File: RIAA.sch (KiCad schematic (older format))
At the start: 34 parts, among them U1 NE5532

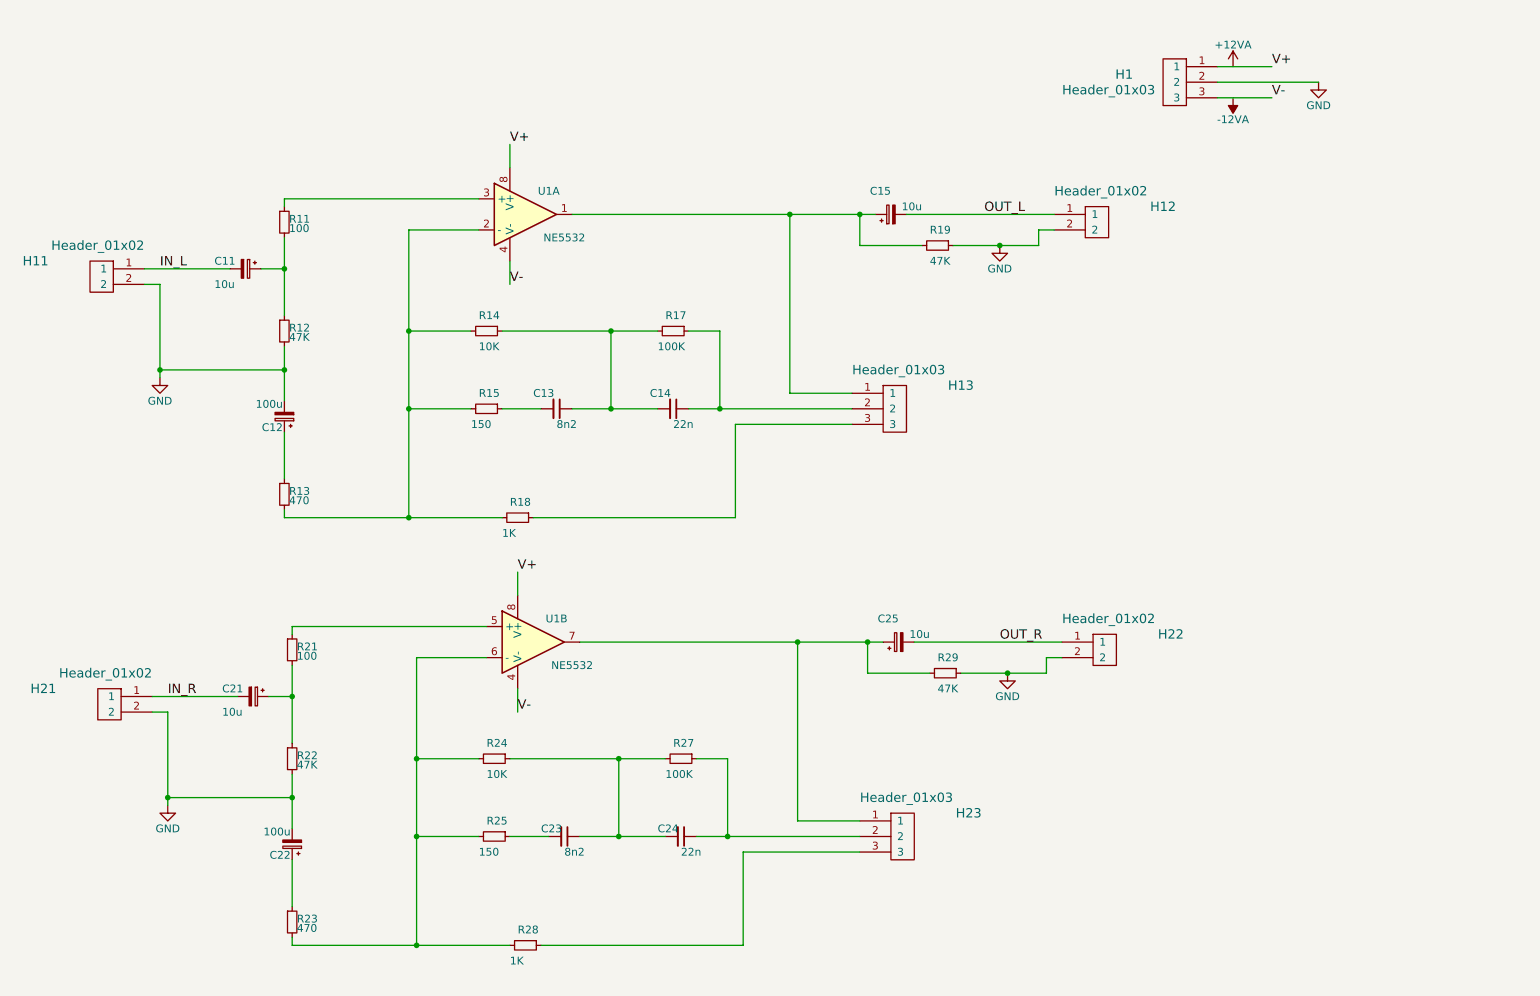
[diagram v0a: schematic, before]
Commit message: Partial update to add Molex connector for the switch connection
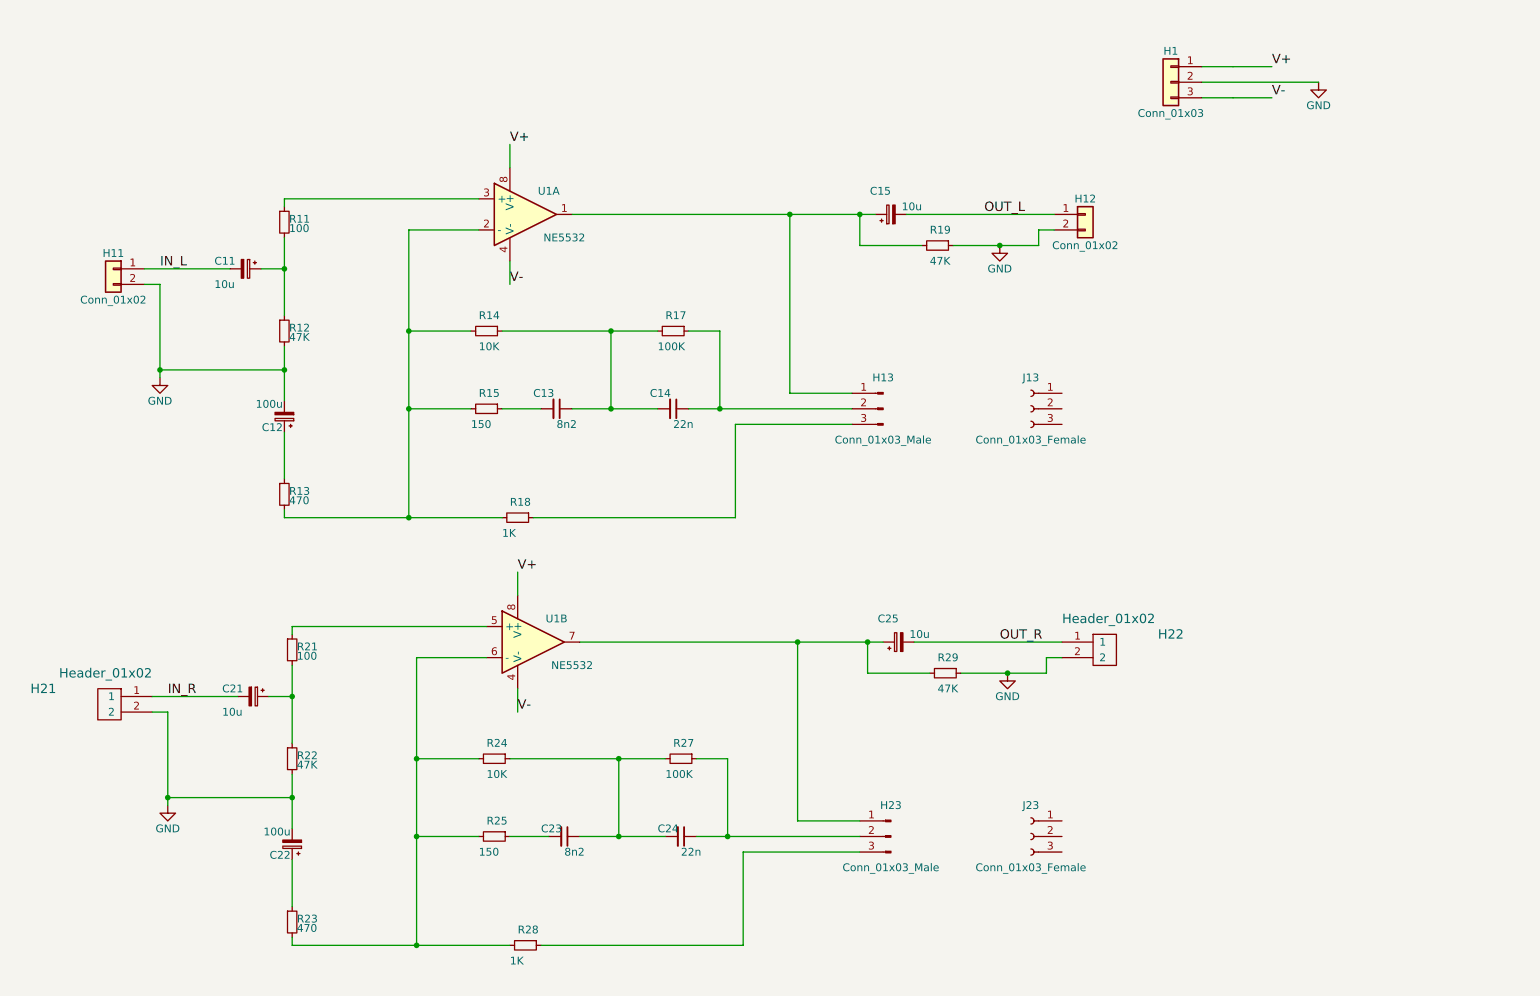
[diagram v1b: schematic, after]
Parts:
- removed H1, H13, H23: Header_01x03, Pin_Headers:Pin_Header_Straight_1x03, symbol Header_01x03
- removed H11, H12: Header_01x02, Pin_Headers:Pin_Header_Straight_1x02, symbol Header_01x02
- added H1: Conn_01x03, symbol Conn_01x03
- added H11, H12: Conn_01x02, symbol Conn_01x02
- added H13, H23: Conn_01x03_Male, Connectors_Molex:Molex_KK-6410-03_03x2.54mm_Straight, symbol Conn_01x03_Male
- added J13, J23: Conn_01x03_Female, symbol Conn_01x03_Female
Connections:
- net GND: now also H1.2 (Pin_2), H11.2 (Pin_2), H12.2 (Pin_2)
- net IN_L: now also H11.1 (Pin_1)
- net OUT_L: now also H12.1 (Pin_1)
- net V+: now also H1.1 (Pin_1)
- net V-: now also H1.3 (Pin_3)
- net at C15.1, R19.2, U1.1: now also H13.1 (Pin_1)
- net at C14.1, R17.1: now also H13.2 (Pin_2)
- net at R18.1: now also H13.3 (Pin_3)
- net at C25.1, R29.2, U1.7: now also H23.1 (Pin_1)
- net at C24.1, R27.1: now also H23.2 (Pin_2)
- net at R28.1: now also H23.3 (Pin_3)

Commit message: Add OpAmp references
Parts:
- U1: Description (none) -> Operational Amplifiers - Op Amps Dual Low Noise; Distributor (none) -> Mouser; Distributor Part # (none) -> 595-NE5532P; Manufacturer (none) -> Texas Instruments; Package (none) -> 8-PDIP
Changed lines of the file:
@@
 F 1 "NE5532" H 4550 1950 50  0000 C CNN
 F 2 "Housings_DIP:DIP-8_W7.62mm_LongPads" H 4300 2100 50  0001 C CNN
-F 3 "" H 4300 2100 50  0000 C CNN
+F 3 "http://www.ti.com/lit/gpn/ne5532" H 4300 2100 50  0001 C CNN
 F 4 "NE5532P" H 4300 2100 60  0001 C CNN "Mfg_Part_No"
+F 5 "Operational Amplifiers - Op Amps Dual Low Noise" H 4300 2100 60  0001 C CNN "Description"
+F 6 "Texas Instruments" H 4300 2100 60  0001 C CNN "Manufacturer"
+F 7 "Mouser" H 4300 2100 60  0001 C CNN "Distributor"
+F 8 "595-NE5532P" H 4300 2100 60  0001 C CNN "Distributor Part #"
+F 9 "8-PDIP" H 4300 2100 60  0001 C CNN "Package"
 	1    4300 2100
 	1    0    0    -1
@@
 F 4 "CCF07470RGKE36CCF07470RGKE36CCF07470RGKE36" H 2800 6650 60  0001 C CNN "Mfg_Part_No"
 	1    2800 6650
-	1    0    0    -1
-$EndComp
-$Comp
-L NE5532 U1
-U 2 1 571FB127
-P 4350 4850
-F 0 "U1" H 4500 5000 50  0000 C CNN
-F 1 "NE5532" H 4600 4700 50  0000 C CNN
-F 2 "Housings_DIP:DIP-8_W7.62mm_LongPads" H 4350 4850 50  0001 C CNN
-F 3 "" H 4350 4850 50  0000 C CNN
-F 4 "NE5532P" H 4350 4850 60  0001 C CNN "Mfg_Part_No"
-	2    4350 4850
 	1    0    0    -1
 $EndComp
@@
 	-1   0    0    -1
 $EndComp
+$Comp
+L NE5532 U1
+U 2 1 5A14798A
+P 4350 4850
+F 0 "U1" H 4500 5000 50  0000 C CNN
+F 1 "NE5532" H 4600 4700 50  0000 C CNN
+F 2 "Housings_DIP:DIP-8_W7.62mm_LongPads" H 4350 4850 50  0001 C CNN
+F 3 "http://www.ti.com/lit/gpn/ne5532" H 4350 4850 50  0001 C CNN
+F 4 "NE5532P" H 4350 4850 60  0001 C CNN "Mfg_Part_No"
+F 5 "Operational Amplifiers - Op Amps Dual Low Noise" H 4350 4850 60  0001 C CNN "Description"
+F 6 "Texas Instruments" H 4350 4850 60  0001 C CNN "Manufacturer"
+F 7 "Mouser" H 4350 4850 60  0001 C CNN "Distributor"
+F 8 "595-NE5532P" H 4350 4850 60  0001 C CNN "Distributor Part #"
+F 9 "8-PDIP" H 4350 4850 60  0001 C CNN "Package"
+	2    4350 4850
+	1    0    0    -1
+$EndComp
 $EndSCHEMATC

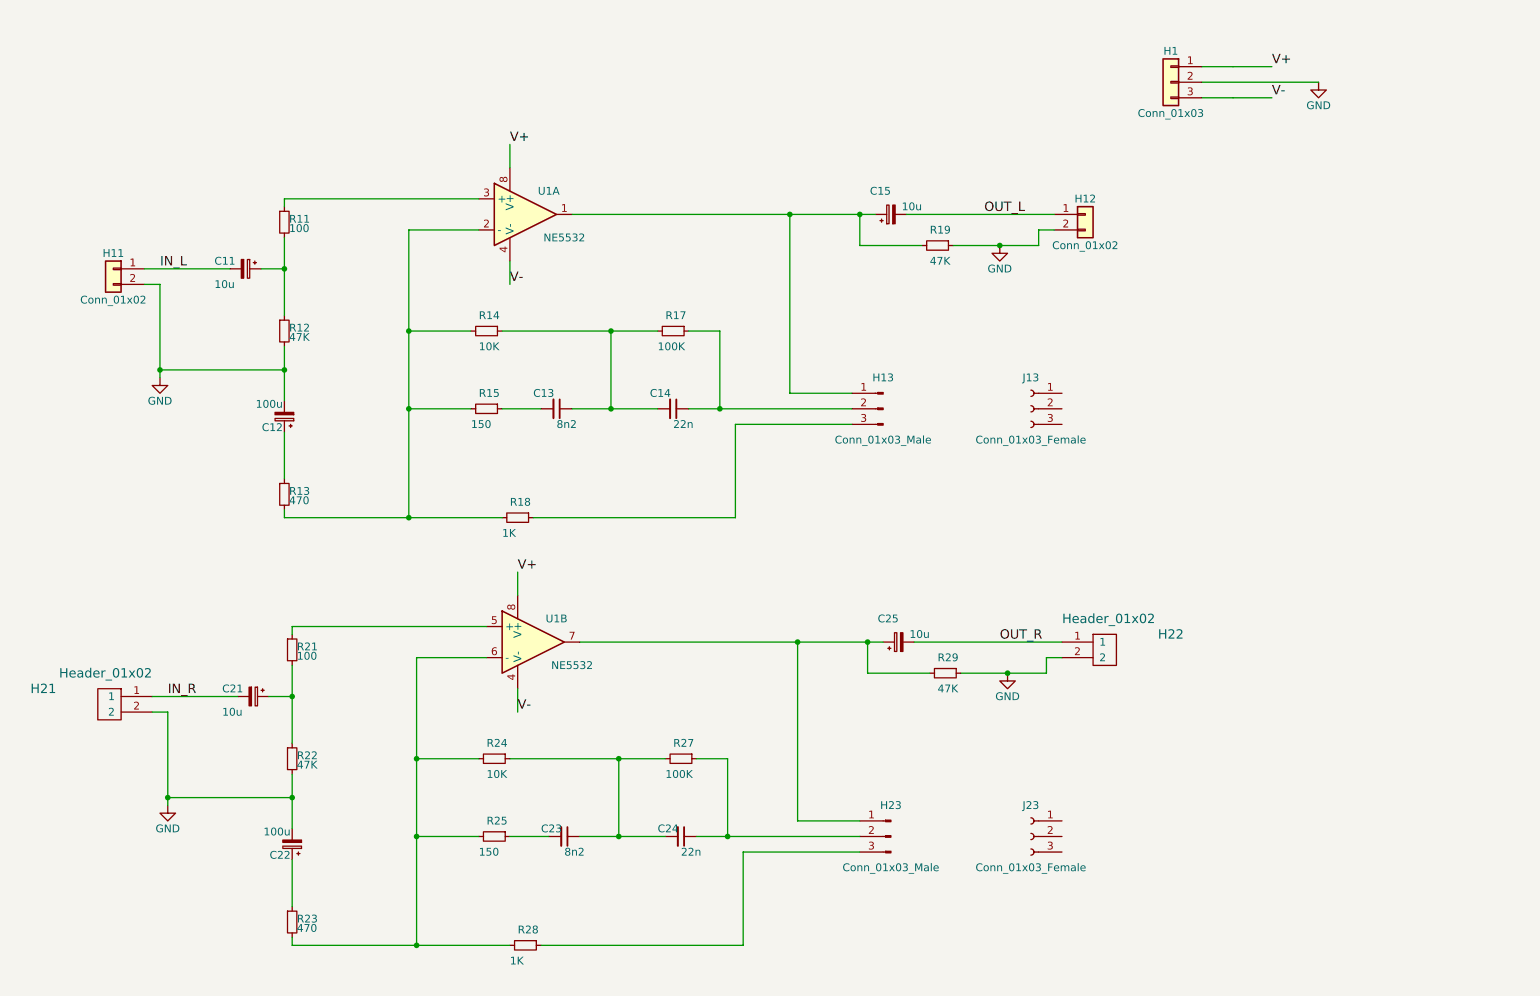
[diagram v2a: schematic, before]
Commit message: Adding switches for line/phono input commutation
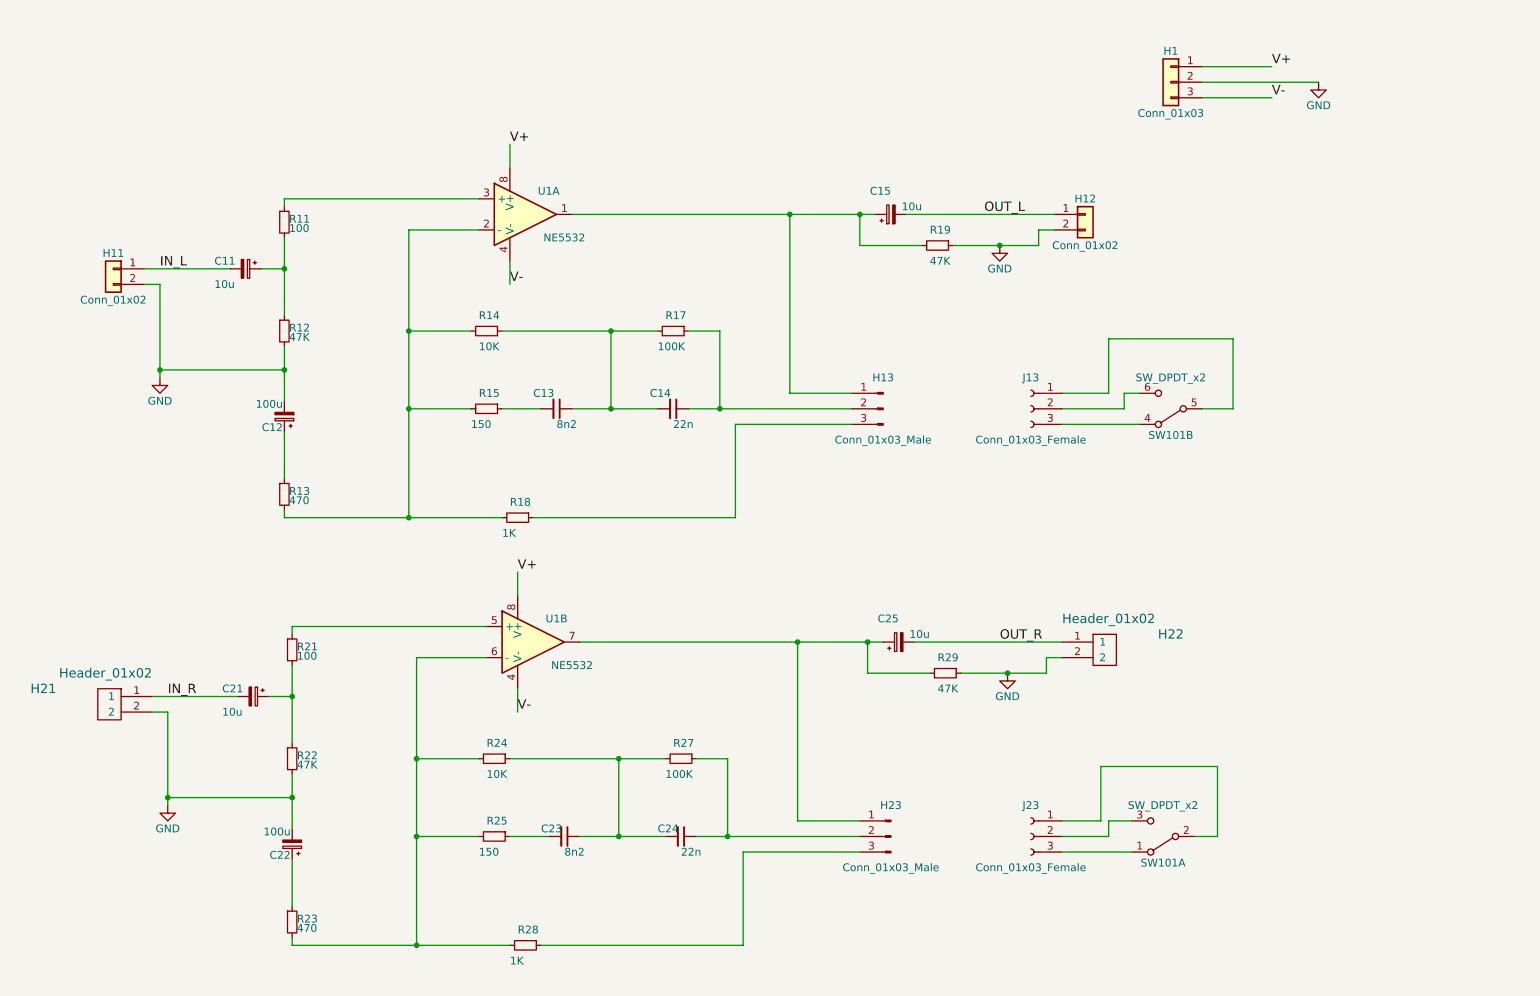
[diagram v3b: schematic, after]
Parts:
- added SW101: SW_DPDT_x2, symbol SW_DPDT_x2
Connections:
- net at J23.1 (Pin_1): now also SW101.2 (B)
- net at J23.2 (Pin_2): now also SW101.3 (C)
- net at J23.3 (Pin_3): now also SW101.1 (A)
- net at J13.1 (Pin_1): now also SW101.5 (B)
- net at J13.2 (Pin_2): now also SW101.6 (C)
- net at J13.3 (Pin_3): now also SW101.4 (A)
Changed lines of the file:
@@
 LIBS:contrib
 LIBS:valves
+LIBS:switches
 LIBS:RIAA-cache
 EELAYER 25 0
@@
 $EndComp
 $Comp
-L GND #PWR01
+L GND #PWR101
 U 1 1 571FAC30
 P 1950 3150
-F 0 "#PWR01" H 1950 2900 50  0001 C CNN
+F 0 "#PWR101" H 1950 2900 50  0001 C CNN
 F 1 "GND" H 1950 3000 50  0000 C CNN
 F 2 "" H 1950 3150 50  0000 C CNN
@@
 	1850 2550 1950 2550
 Wire Wire Line
-	1950 2550 1950 3100
-Wire Wire Line
-	1950 3100 1950 3150
+	1950 2550 1950 3150
 Wire Wire Line
 	1850 2450 2400 2450
@@
 	2600 2450 2750 2450
 Wire Wire Line
-	2750 2250 2750 2450
-Wire Wire Line
-	2750 2450 2750 2750
+	2750 2250 2750 2750
 Connection ~ 2750 2450
 Wire Wire Line
-	2750 2950 2750 3100
-Wire Wire Line
-	2750 3100 2750 3300
+	2750 2950 2750 3300
 Wire Wire Line
 	2750 3500 2750 3800
@@
 $EndComp
 Wire Wire Line
-	5350 3350 5550 3350
-Wire Wire Line
-	5550 3350 6400 3350
+	5350 3350 6400 3350
 Wire Wire Line
 	5350 2850 5550 2850
@@
 Connection ~ 5550 3350
 Wire Wire Line
-	4150 2850 4850 2850
-Wire Wire Line
-	4850 2850 5150 2850
-Wire Wire Line
-	4600 3350 4850 3350
-Wire Wire Line
-	4850 3350 5150 3350
+	4150 2850 5150 2850
+Wire Wire Line
+	4600 3350 5150 3350
 Wire Wire Line
 	4850 3350 4850 2850
@@
 	3950 2850 3550 2850
 Wire Wire Line
-	3550 2200 3550 2850
-Wire Wire Line
-	3550 2850 3550 3350
-Wire Wire Line
-	3550 3350 3550 4050
+	3550 2200 3550 4050
 Wire Wire Line
 	3550 3350 3950 3350
@@
 	2750 4000 2750 4050
 Wire Wire Line
-	2750 4050 3550 4050
-Wire Wire Line
-	3550 4050 4150 4050
+	2750 4050 4150 4050
 Wire Wire Line
 	4350 4050 5650 4050
@@
 	5650 3450 6400 3450
 Wire Wire Line
-	8650 1150 8850 1150
-Wire Wire Line
-	8850 1150 9100 1150
-Wire Wire Line
-	8650 1350 8850 1350
-Wire Wire Line
-	8850 1350 9100 1350
+	8650 1150 9100 1150
+Wire Wire Line
+	8650 1350 9100 1350
 Text Label 9100 1150 0    60   ~ 0
 V+
@@
 	2750 2000 4000 2000
 Wire Wire Line
-	4600 2100 6000 2100
-Wire Wire Line
-	6000 2100 6450 2100
-Wire Wire Line
-	6450 2100 6550 2100
+	4600 2100 6550 2100
 Wire Wire Line
 	6000 2100 6000 3250
@@
 $EndComp
 $Comp
-L GND #PWR04
+L GND #PWR103
 U 1 1 571FAC4B
 P 7350 2300
-F 0 "#PWR04" H 7350 2050 50  0001 C CNN
+F 0 "#PWR103" H 7350 2050 50  0001 C CNN
 F 1 "GND" H 7350 2150 50  0000 C CNN
 F 2 "" H 7350 2300 50  0000 C CNN
@@
 $EndComp
 Wire Wire Line
-	7050 2300 7350 2300
-Wire Wire Line
-	7350 2300 7600 2300
+	7050 2300 7600 2300
 Wire Wire Line
 	7700 2200 7600 2200
@@
 $EndComp
 $Comp
-L GND #PWR05
+L GND #PWR102
 U 1 1 571FB0FD
 P 2000 5900
-F 0 "#PWR05" H 2000 5650 50  0001 C CNN
+F 0 "#PWR102" H 2000 5650 50  0001 C CNN
 F 1 "GND" H 2000 5750 50  0000 C CNN
 F 2 "" H 2000 5900 50  0000 C CNN
@@
 	1900 5300 2000 5300
 Wire Wire Line
-	2000 5300 2000 5850
-Wire Wire Line
-	2000 5850 2000 5900
+	2000 5300 2000 5900
 Wire Wire Line
 	1900 5200 2450 5200
@@
 	2650 5200 2800 5200
 Wire Wire Line
-	2800 5000 2800 5200
-Wire Wire Line
-	2800 5200 2800 5500
+	2800 5000 2800 5500
 Connection ~ 2800 5200
 Wire Wire Line
-	2800 5700 2800 5850
-Wire Wire Line
-	2800 5850 2800 6050
+	2800 5700 2800 6050
 Wire Wire Line
 	2800 6250 2800 6550
@@
 $EndComp
 Wire Wire Line
-	5400 6100 5600 6100
-Wire Wire Line
-	5600 6100 6450 6100
+	5400 6100 6450 6100
 Wire Wire Line
 	5400 5600 5600 5600
@@
 Connection ~ 5600 6100
 Wire Wire Line
-	4200 5600 4900 5600
-Wire Wire Line
-	4900 5600 5200 5600
-Wire Wire Line
-	4650 6100 4900 6100
-Wire Wire Line
-	4900 6100 5200 6100
+	4200 5600 5200 5600
+Wire Wire Line
+	4650 6100 5200 6100
 Wire Wire Line
 	4900 6100 4900 5600
@@
 	4000 5600 3600 5600
 Wire Wire Line
-	3600 4950 3600 5600
-Wire Wire Line
-	3600 5600 3600 6100
-Wire Wire Line
-	3600 6100 3600 6800
+	3600 4950 3600 6800
 Wire Wire Line
 	3600 6100 4000 6100
@@
 	2800 6750 2800 6800
 Wire Wire Line
-	2800 6800 3600 6800
-Wire Wire Line
-	3600 6800 4200 6800
+	2800 6800 4200 6800
 Wire Wire Line
 	4400 6800 5700 6800
@@
 	2800 4750 4050 4750
 Wire Wire Line
-	4650 4850 6050 4850
-Wire Wire Line
-	6050 4850 6500 4850
-Wire Wire Line
-	6500 4850 6600 4850
+	4650 4850 6600 4850
 Wire Wire Line
 	6050 4850 6050 6000
@@
 $EndComp
 $Comp
-L GND #PWR06
+L GND #PWR104
 U 1 1 571FB199
 P 7400 5050
-F 0 "#PWR06" H 7400 4800 50  0001 C CNN
+F 0 "#PWR104" H 7400 4800 50  0001 C CNN
 F 1 "GND" H 7400 4900 50  0000 C CNN
 F 2 "" H 7400 5050 50  0000 C CNN
@@
 $EndComp
 Wire Wire Line
-	7100 5050 7400 5050
-Wire Wire Line
-	7400 5050 7650 5050
+	7100 5050 7650 5050
 Wire Wire Line
 	7750 4950 7650 4950
@@
 	6800 4850 7750 4850
 $Comp
-L GND #PWR07
+L GND #PWR105
 U 1 1 5724D462
 P 9400 1250
-F 0 "#PWR07" H 9400 1000 50  0001 C CNN
+F 0 "#PWR105" H 9400 1000 50  0001 C CNN
 F 1 "GND" H 9400 1100 50  0000 C CNN
 F 2 "" H 9400 1250 50  0000 C CNN
@@
 	1    0    0    -1
 $EndComp
+$Comp
+L SW_DPDT_x2 SW101
+U 2 1 5A148165
+P 8450 3350
+F 0 "SW101" H 8450 3520 50  0000 C CNN
+F 1 "SW_DPDT_x2" H 8450 3150 50  0000 C CNN
+F 2 "" H 8450 3350 50  0001 C CNN
+F 3 "http://www.mouser.com/ds/2/418/NG_CD_1825138_A5_baseFilename-660361.pdf" H 8450 3350 50  0001 C CNN
+F 4 "A201SYZQ04" H 8450 3350 60  0001 C CNN "Mfg_Part_No"
+F 5 "Toggle Switches DP ON-ON LNG BAT LUG TOGGLE SWITCH" H 8450 3350 60  0001 C CNN "Description"
+F 6 "TE Connectivity / Alcoswitch" H 8450 3350 60  0001 C CNN "Manufacturer"
+F 7 "Mouser" H 8450 3350 60  0001 C CNN "Distributor"
+F 8 "506-A201SYZQ04" H 8450 3350 60  0001 C CNN "Distributor Part #"
+	2    8450 3350
+	-1   0    0    1
+$EndComp
+$Comp
+L SW_DPDT_x2 SW101
+U 1 1 5A14863A
+P 8400 6100
+F 0 "SW101" H 8400 6270 50  0000 C CNN
+F 1 "SW_DPDT_x2" H 8400 5900 50  0000 C CNN
+F 2 "" H 8400 6100 50  0001 C CNN
+F 3 "http://www.mouser.com/ds/2/418/NG_CD_1825138_A5_baseFilename-660361.pdf" H 8400 6100 50  0001 C CNN
+F 4 "A201SYZQ04" H 8400 6100 60  0001 C CNN "Mfg_Part_No"
+F 5 "Toggle Switches DP ON-ON LNG BAT LUG TOGGLE SWITCH" H 8400 6100 60  0001 C CNN "Description"
+F 6 "TE Connectivity / Alcoswitch" H 8400 6100 60  0001 C CNN "Manufacturer"
+F 7 "Mouser" H 8400 6100 60  0001 C CNN "Distributor"
+F 8 "506-A201SYZQ04" H 8400 6100 60  0001 C CNN "Distributor Part #"
+F 9 "0402" H 8400 6100 60  0001 C CNN "Package"
+	1    8400 6100
+	-1   0    0    1
+$EndComp
+Wire Wire Line
+	7750 6000 8000 6000
+Wire Wire Line
+	8000 6000 8000 5650
+Wire Wire Line
+	8000 5650 8750 5650
+Wire Wire Line
+	8750 5650 8750 6100
+Wire Wire Line
+	8750 6100 8600 6100
+Wire Wire Line
+	8200 6000 8050 6000
+Wire Wire Line
+	8050 6000 8050 6100
+Wire Wire Line
+	8050 6100 7750 6100
+Wire Wire Line
+	7750 6200 8200 6200
+Wire Wire Line
+	7750 3250 8050 3250
+Wire Wire Line
+	8050 3250 8050 2900
+Wire Wire Line
+	8050 2900 8850 2900
+Wire Wire Line
+	8850 2900 8850 3350
+Wire Wire Line
+	8850 3350 8650 3350
+Wire Wire Line
+	8250 3250 8150 3250
+Wire Wire Line
+	8150 3250 8150 3350
+Wire Wire Line
+	8150 3350 7750 3350
+Wire Wire Line
+	7750 3450 8250 3450
 $EndSCHEMATC
